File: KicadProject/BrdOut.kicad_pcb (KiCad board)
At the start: 4 copper layers, 80 x 51 mm, 60 parts, among them J1 USB, J2 Debug_Header, J3 4_Pos, J4 XLR, Q1 BJT_PNP, SW1 Button, SW2 Button, U1 LPC11U14, U2 ZLDO1117, U3 1G_NAND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

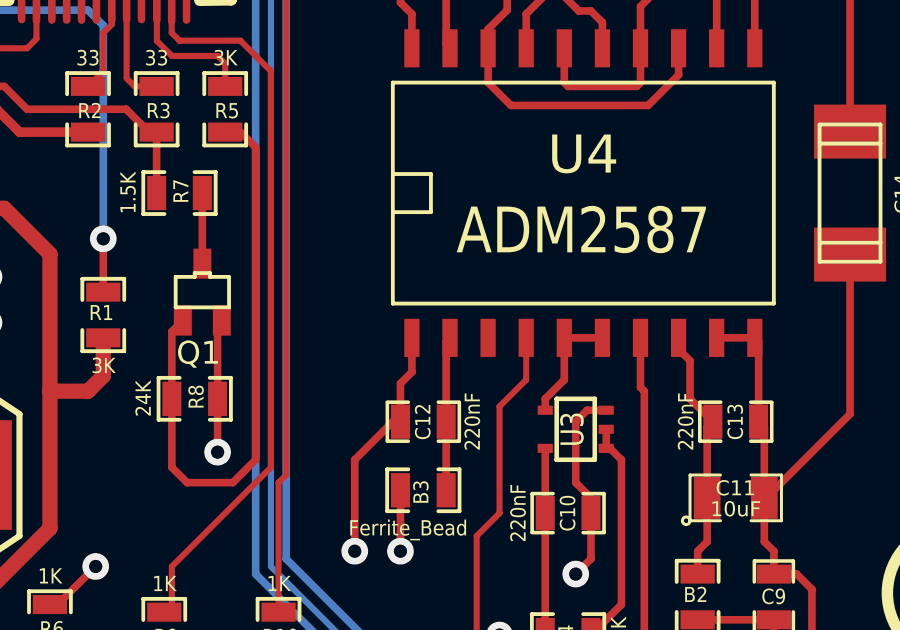
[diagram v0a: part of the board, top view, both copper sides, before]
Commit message: Add missing ground connection on ADM2587.
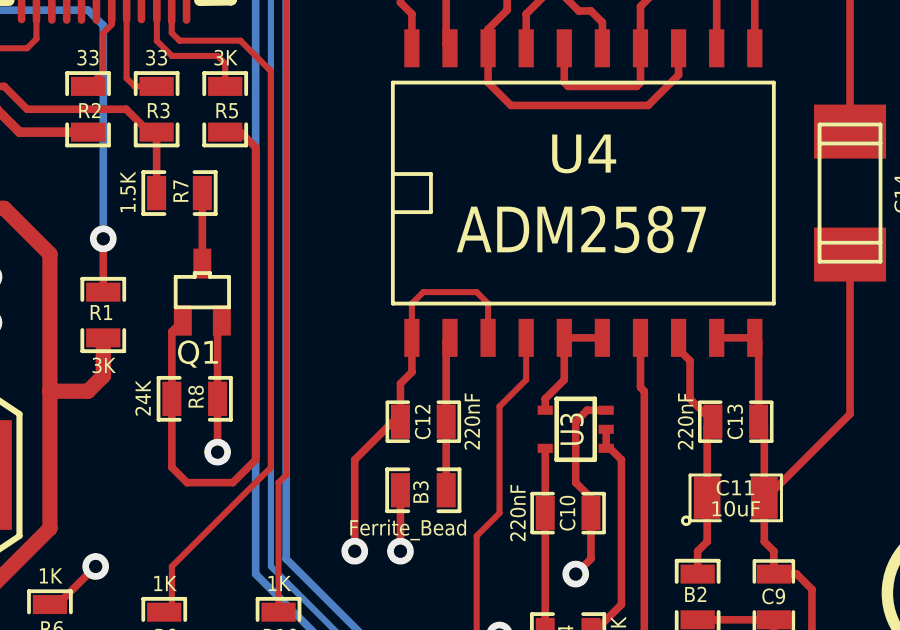
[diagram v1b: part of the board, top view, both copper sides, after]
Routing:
- net GND: track 132.2 -> 137.4 mm
